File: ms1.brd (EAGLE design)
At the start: 100 x 100 mm, 125 parts, among them IC1 MAX3232EUE, J1 POWERPOLE_POWER25A, J10 RS485, J11 I2C, J12 TTL_SERIAL, J13 Radio, J14 RS232, J2 RAIN, J3 ADC1, J4 ON, J5 D1, J6 D2, J7 ADC2, J8 LED-EN, Q1 DMG6602SVT, Q2 DMG6602SVT, Q3 DMG6602SVT, Q4 DMG6602SVT, U1 LT1934ES6TRMPBF, U2 LT1934ES6TRMPBF, U3 DS3231SN, U4 ISL3179EIBZ, X1 KUSBVX-BS1N

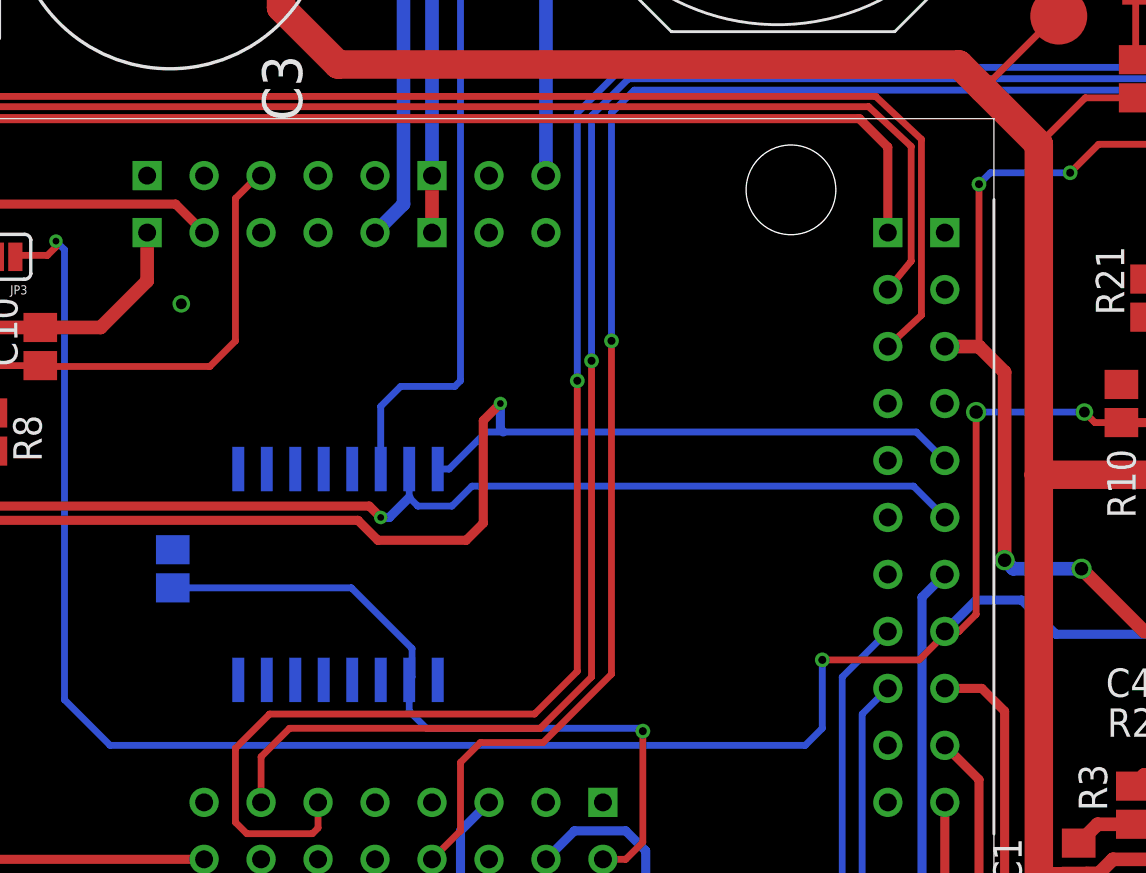
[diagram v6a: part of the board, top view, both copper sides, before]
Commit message: fixes #4 all the same pins on z1 are now linked
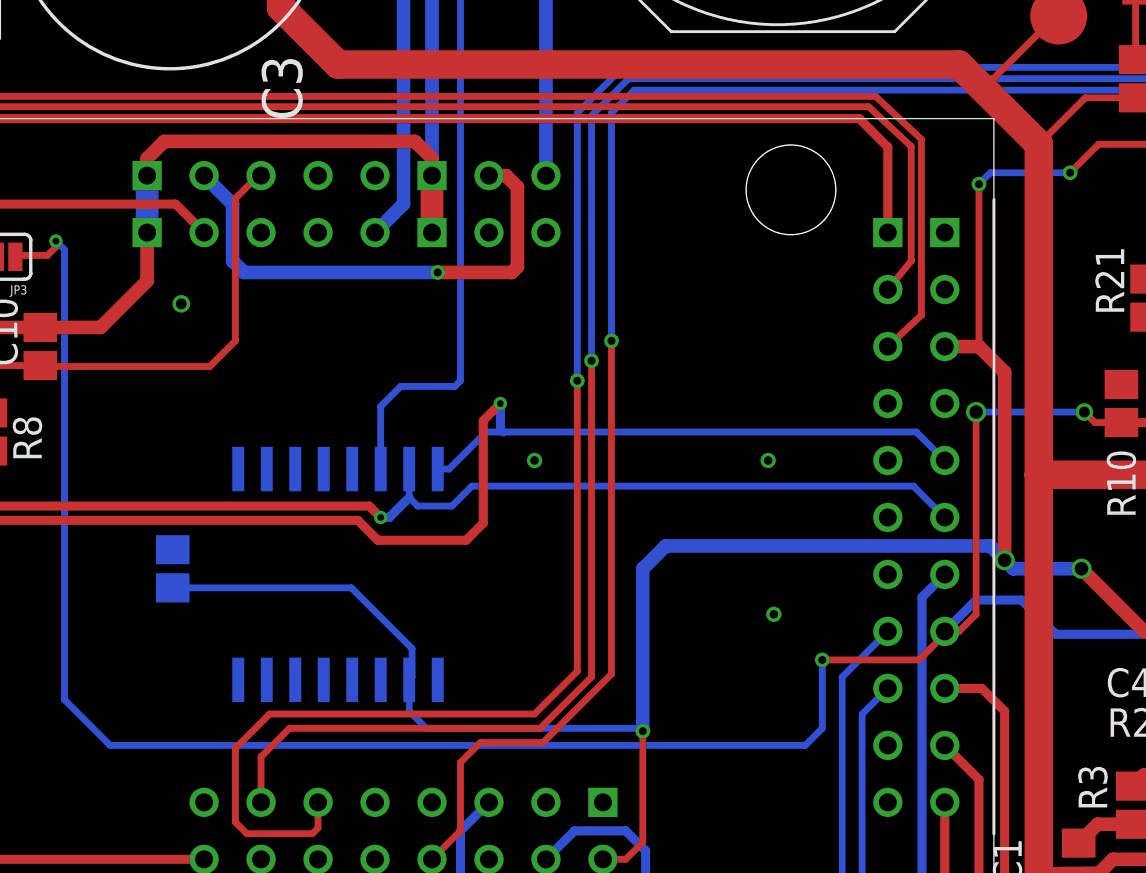
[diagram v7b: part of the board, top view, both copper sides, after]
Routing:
- net VCC_3V3: track 221.6 -> 245.7 mm
- net ADC_3V3: track 0.00 -> 22.4 mm, vias 0 -> 1
- net AGND: track 95.5 -> 113.0 mm
- net GND: vias 21 -> 24
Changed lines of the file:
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@@
 <setting verticaltext="up"/>
 </settings>
-<grid distance="20" unitdist="mil" unit="mil" style="lines" multiple="1" display="yes" altdistance="1" altunitdist="mil" altunit="mil"/>
+<grid distance="10" unitdist="mil" unit="mil" style="lines" multiple="1" display="yes" altdistance="1" altunitdist="mil" altunit="mil"/>
 <layers>
 <layer number="1" name="Top" color="4" fill="1" visible="yes" active="yes"/>
@@
 <contactref element="R4" pad="1"/>
 <contactref element="Q1" pad="P$5"/>
-<contactref element="U$5" pad="B24" route="any" routetag="DGND"/>
-<contactref element="U$5" pad="C39" route="any" routetag="DGND"/>
+<contactref element="U$5" pad="B24"/>
+<contactref element="U$5" pad="C39"/>
 <contactref element="U3" pad="5"/>
 <contactref element="U3" pad="7"/>
@@
 <via x="67.691" y="86.995" extent="1-16" drill="0.4826" shape="square"/>
 <contactref element="JP5" pad="1"/>
+<via x="38.862" y="58.42" extent="1-16" drill="0.381" shape="square"/>
+<via x="49.276" y="58.42" extent="1-16" drill="0.381" shape="square"/>
+<via x="49.53" y="51.562" extent="1-16" drill="0.381" shape="square"/>
 </signal>
 <signal name="VCC">
@@
 <contactref element="R13" pad="2"/>
 <contactref element="R18" pad="2"/>
-<contactref element="U$5" pad="B22" route="any" routetag="D-3V"/>
-<contactref element="U$5" pad="C40" route="any" routetag="D-3V"/>
+<contactref element="U$5" pad="B22"/>
+<contactref element="U$5" pad="C40"/>
 <contactref element="U3" pad="2"/>
 <contactref element="C19" pad="2"/>
@@
 <wire x1="43.688" y1="41.402" x2="42.926" y2="40.64" width="0.3048" layer="1"/>
 <wire x1="42.926" y1="40.64" x2="41.91" y2="40.64" width="0.3048" layer="1"/>
+<wire x1="59.817" y1="53.975" x2="59.182" y2="54.61" width="0.6096" layer="16"/>
+<wire x1="59.182" y1="54.61" x2="44.704" y2="54.61" width="0.6096" layer="16"/>
+<wire x1="44.704" y1="54.61" x2="43.688" y2="53.594" width="0.6096" layer="16"/>
+<wire x1="43.688" y1="53.594" x2="43.688" y2="46.355" width="0.6096" layer="16"/>
 </signal>
 <signal name="N$1">
@@
 <contactref element="C10" pad="2"/>
 <contactref element="R9" pad="1"/>
-<contactref element="U$5" pad="A1" route="any" routetag="AGND"/>
-<contactref element="U$5" pad="A2" route="any" routetag="AGND"/>
-<contactref element="U$5" pad="A11" route="any" routetag="AGND"/>
-<contactref element="U$5" pad="A12" route="any" routetag="AGND"/>
+<contactref element="U$5" pad="A1"/>
+<contactref element="U$5" pad="A2"/>
+<contactref element="U$5" pad="A11"/>
+<contactref element="U$5" pad="A12"/>
 <contactref element="AGND" pad="TP"/>
 <contactref element="J3" pad="3"/>
@@
 <wire x1="66.167" y1="85.217" x2="36.195" y2="85.217" width="0.6096" layer="1"/>
 <wire x1="36.195" y1="85.217" x2="34.29" y2="83.312" width="0.6096" layer="1"/>
-<wire x1="34.29" y1="71.12" x2="34.29" y2="68.453" width="0.6096" layer="1"/>
 <wire x1="12.065" y1="64.35" x2="16.8275" y2="64.35" width="0.6096" layer="1"/>
 <wire x1="16.8275" y1="64.35" x2="19.519" y2="64.35" width="0.6096" layer="1"/>
@@
 <wire x1="29.718" y1="86.106" x2="32.512" y2="83.312" width="0.3048" layer="1"/>
 <wire x1="32.512" y1="83.312" x2="34.29" y2="83.312" width="0.3048" layer="1"/>
+<wire x1="34.29" y1="71.12" x2="34.29" y2="68.58" width="1.016" layer="1"/>
+<wire x1="21.59" y1="71.12" x2="21.59" y2="68.58" width="1.016" layer="16"/>
+<wire x1="21.59" y1="71.12" x2="21.336" y2="71.12" width="0.6096" layer="16"/>
+<wire x1="34.29" y1="71.12" x2="34.29" y2="71.882" width="0.6096" layer="1"/>
+<wire x1="34.29" y1="71.882" x2="33.528" y2="72.644" width="0.6096" layer="1"/>
+<wire x1="33.528" y1="72.644" x2="22.352" y2="72.644" width="0.6096" layer="1"/>
+<wire x1="22.352" y1="72.644" x2="21.59" y2="71.882" width="0.6096" layer="1"/>
+<wire x1="21.59" y1="71.882" x2="21.59" y2="71.12" width="0.6096" layer="1"/>
 </signal>
 <signal name="SCL">
@@
 </signal>
 <signal name="USB_VCC">
-<contactref element="U$5" pad="A3" route="any" routetag="USB-5V"/>
-<contactref element="U$5" pad="A13" route="any" routetag="USB-5V"/>
-<contactref element="U$5" pad="B23" route="any" routetag="USB-5V"/>
+<contactref element="U$5" pad="A3" route="any" routetag="G$1.USB-5V"/>
+<contactref element="U$5" pad="A13" route="any" routetag="G$1.USB-5V"/>
+<contactref element="U$5" pad="B23" route="any" routetag="G$1.USB-5V"/>
 <contactref element="X1" pad="1"/>
 <wire x1="11.2725" y1="81.935" x2="11.2725" y2="75.7225" width="0.4064" layer="1"/>
@@
 </signal>
 <signal name="ADC_3V3">
-<contactref element="U$5" pad="A4" route="any" routetag="ADC_3V3"/>
-<contactref element="U$5" pad="A14" route="any" routetag="ADC_3V3"/>
+<contactref element="U$5" pad="A4"/>
+<contactref element="U$5" pad="A14"/>
+<wire x1="24.13" y1="71.12" x2="25.4" y2="69.85" width="0.6096" layer="16"/>
+<wire x1="25.4" y1="69.85" x2="25.4" y2="67.31" width="0.6096" layer="16"/>
+<wire x1="25.4" y1="67.31" x2="25.908" y2="66.802" width="0.6096" layer="16"/>
+<wire x1="25.908" y1="66.802" x2="34.544" y2="66.802" width="0.6096" layer="16"/>
+<via x="34.544" y="66.802" extent="1-16" drill="0.3556"/>
+<wire x1="34.544" y1="66.802" x2="37.846" y2="66.802" width="0.6096" layer="1"/>
+<wire x1="37.846" y1="66.802" x2="38.1" y2="67.056" width="0.6096" layer="1"/>
+<wire x1="38.1" y1="67.056" x2="38.1" y2="70.612" width="0.6096" layer="1"/>
+<wire x1="38.1" y1="70.612" x2="37.592" y2="71.12" width="0.6096" layer="1"/>
+<wire x1="37.592" y1="71.12" x2="36.83" y2="71.12" width="0.6096" layer="1"/>
 </signal>
 <signal name="VCC-3V">
